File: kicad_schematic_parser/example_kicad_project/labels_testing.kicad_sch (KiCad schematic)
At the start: 11 parts, among them J3 Conn_01x04, J4 Conn_01x04, U4 NCP1117-3.3_SOT223

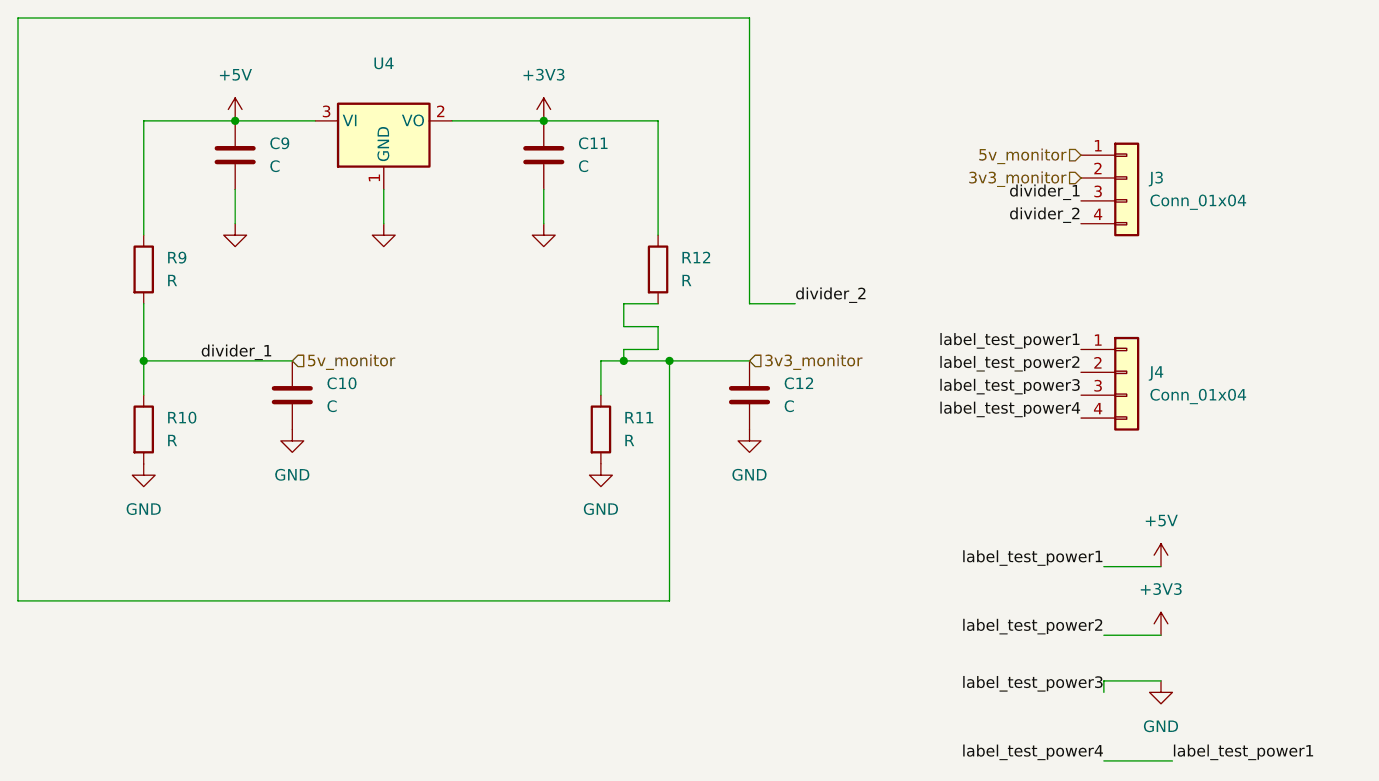
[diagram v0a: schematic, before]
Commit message: simplify label testing.  add errors to README.md
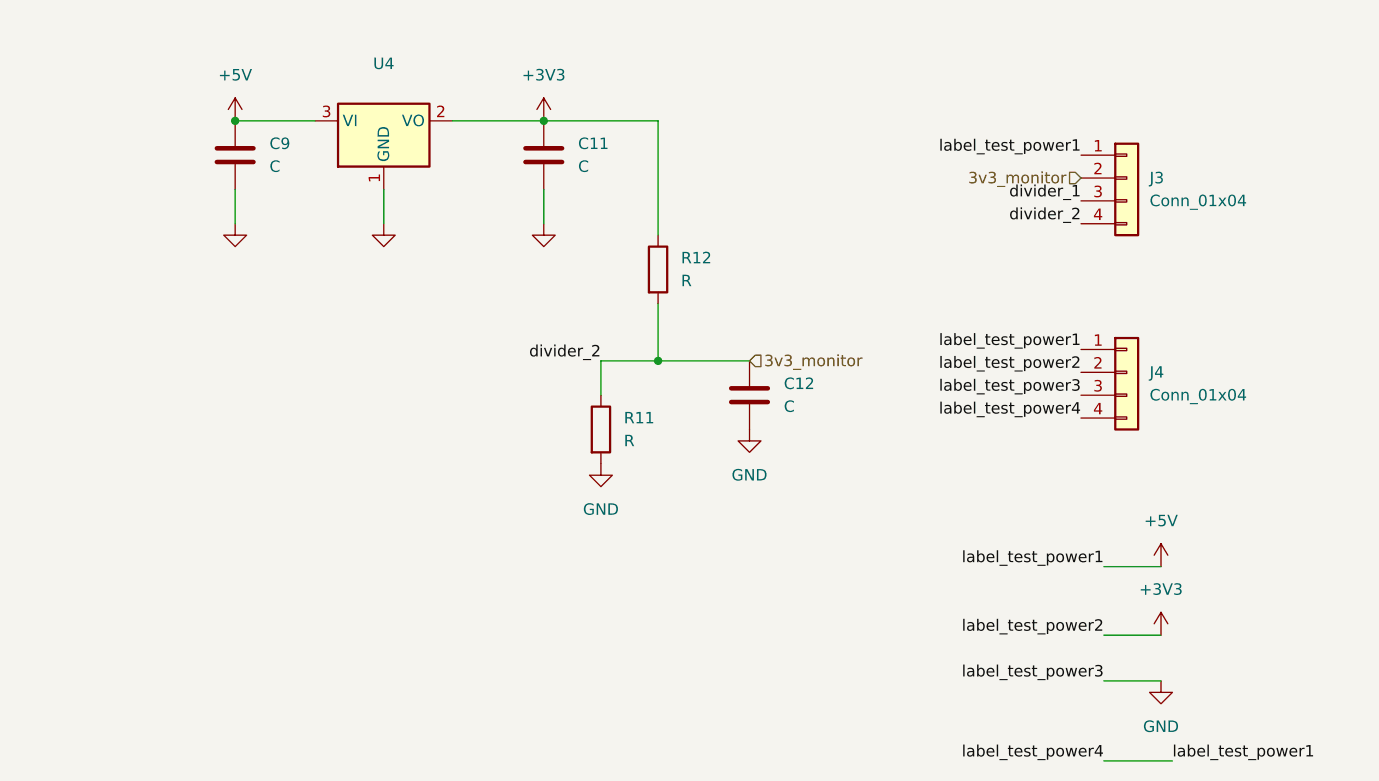
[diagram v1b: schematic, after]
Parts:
- removed C10: C, symbol Device:C
- removed R10, R9: R, Resistor_SMD:R_0603_1608Metric, symbol Device:R
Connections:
- net +5V: now also J3.1 (Pin_1)
- net 5v_monitor renamed divider_1
- net divider_1: no longer J3.1 (Pin_1)
